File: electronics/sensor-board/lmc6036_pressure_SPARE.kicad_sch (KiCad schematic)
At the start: 17 parts, among them U15 LMC6036

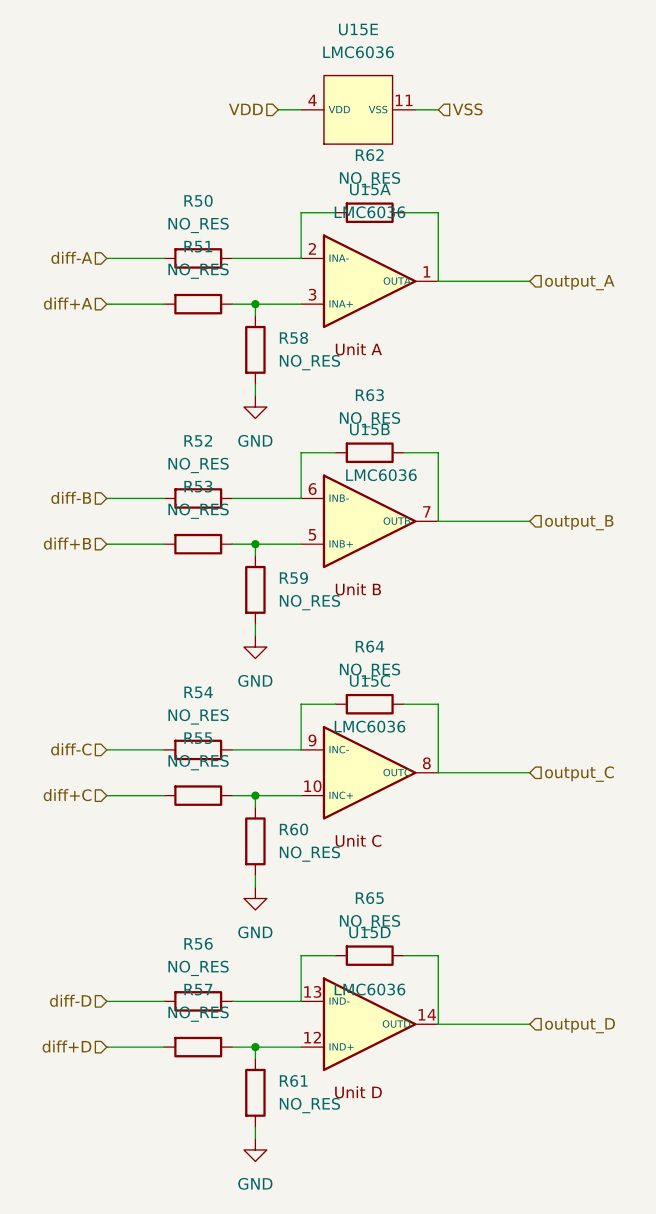
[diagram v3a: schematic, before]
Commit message: updated loadcell amplifier
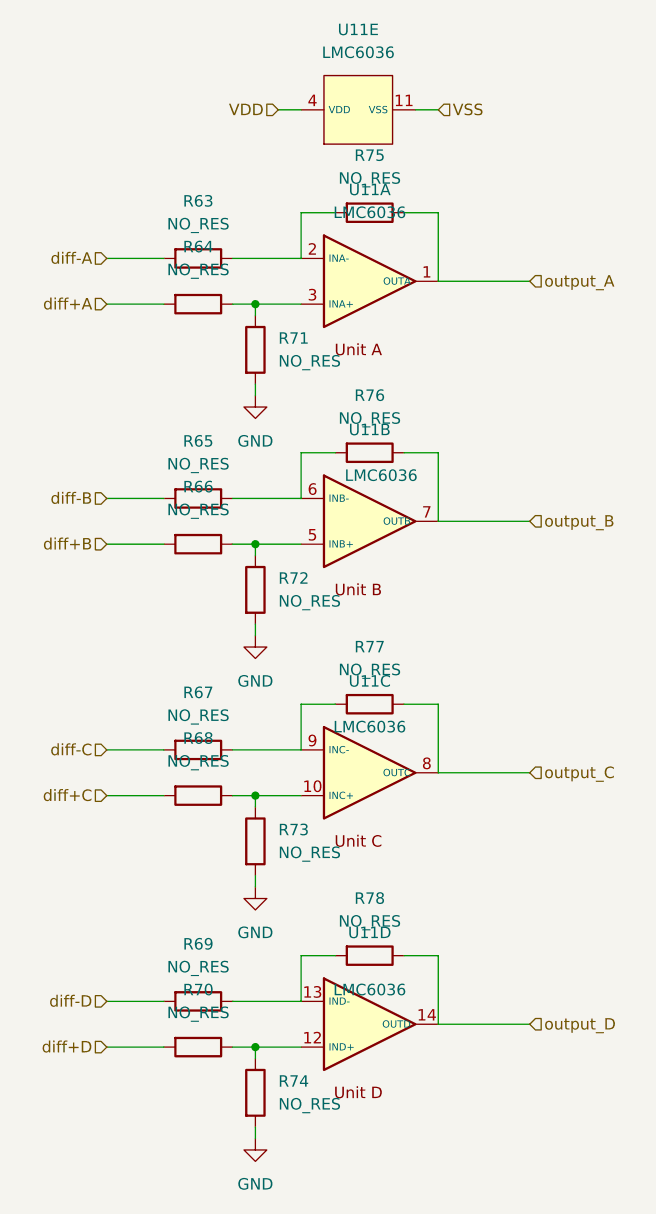
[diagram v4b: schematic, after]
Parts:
- renumbered R50 to R63, R51 to R64, R52 to R65, R53 to R66, R54 to R67, R55 to R68, R56 to R69, R57 to R70, R58 to R71, R59 to R72, R60 to R73, R61 to R74, R62 to R75, R63 to R76, R64 to R77, R65 to R78, U15 to U11
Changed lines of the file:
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@@
   (symbol (lib_id "LMC6036_custom:LMC6036") (at 153.67 63.5 0) (unit 1)
     (in_bom yes) (on_board yes) (fields_autoplaced)
-    (property "Reference" "U15" (id 0) (at 154.94 53.34 0))
+    (property "Reference" "U11" (id 0) (at 154.94 53.34 0))
     (property "Value" "LMC6036" (id 1) (at 154.94 55.88 0))
     (property "Footprint" "LMC6036:SOP65P640X120-14N" (id 2) (at 155.575 63.5 0)
@@
   (symbol (lib_id "Device:R") (at 154.94 55.88 270) (unit 1)
     (in_bom yes) (on_board yes) (fields_autoplaced)
-    (property "Reference" "R62" (id 0) (at 154.94 49.53 90))
+    (property "Reference" "R75" (id 0) (at 154.94 49.53 90))
     (property "Value" "NO_RES" (id 1) (at 154.94 52.07 90))
     (property "Footprint" "Resistor_SMD:R_0603_1608Metric" (id 2) (at 154.94 54.102 90)
@@
   (symbol (lib_id "Device:R") (at 135.89 87.63 270) (unit 1)
     (in_bom yes) (on_board yes) (fields_autoplaced)
-    (property "Reference" "R52" (id 0) (at 135.89 81.28 90))
+    (property "Reference" "R65" (id 0) (at 135.89 81.28 90))
     (property "Value" "NO_RES" (id 1) (at 135.89 83.82 90))
     (property "Footprint" "Resistor_SMD:R_0603_1608Metric" (id 2) (at 135.89 85.852 90)
@@
   (symbol (lib_id "LMC6036_custom:LMC6036") (at 153.67 146.05 0) (unit 4)
     (in_bom yes) (on_board yes)
-    (property "Reference" "U15" (id 0) (at 154.94 135.89 0))
+    (property "Reference" "U11" (id 0) (at 154.94 135.89 0))
     (property "Value" "LMC6036" (id 1) (at 154.94 142.24 0))
     (property "Footprint" "LMC6036:SOP65P640X120-14N" (id 2) (at 155.575 146.05 0)
@@
   (symbol (lib_id "power:GND") (at 142.24 76.2 0) (unit 1)
     (in_bom yes) (on_board yes) (fields_autoplaced)
-    (property "Reference" "#PWR0115" (id 0) (at 142.24 82.55 0)
+    (property "Reference" "#PWR0134" (id 0) (at 142.24 82.55 0)
       (effects (font (size 1.27 1.27)) hide)
     )
@@
   (symbol (lib_id "LMC6036_custom:LMC6036") (at 153.67 118.11 0) (unit 3)
     (in_bom yes) (on_board yes)
-    (property "Reference" "U15" (id 0) (at 154.94 107.95 0))
+    (property "Reference" "U11" (id 0) (at 154.94 107.95 0))
     (property "Value" "LMC6036" (id 1) (at 154.94 113.03 0))
     (property "Footprint" "LMC6036:SOP65P640X120-14N" (id 2) (at 155.575 118.11 0)
@@
   (symbol (lib_id "Device:R") (at 135.89 143.51 270) (unit 1)
     (in_bom yes) (on_board yes) (fields_autoplaced)
-    (property "Reference" "R56" (id 0) (at 135.89 137.16 90))
+    (property "Reference" "R69" (id 0) (at 135.89 137.16 90))
     (property "Value" "NO_RES" (id 1) (at 135.89 139.7 90))
     (property "Footprint" "Resistor_SMD:R_0603_1608Metric" (id 2) (at 135.89 141.732 90)
@@
   (symbol (lib_id "Device:R") (at 142.24 97.79 0) (unit 1)
     (in_bom yes) (on_board yes) (fields_autoplaced)
-    (property "Reference" "R59" (id 0) (at 144.78 96.5199 0)
+    (property "Reference" "R72" (id 0) (at 144.78 96.5199 0)
       (effects (font (size 1.27 1.27)) (justify left))
     )
@@
   (symbol (lib_id "power:GND") (at 142.24 102.87 0) (unit 1)
     (in_bom yes) (on_board yes) (fields_autoplaced)
-    (property "Reference" "#PWR0116" (id 0) (at 142.24 109.22 0)
+    (property "Reference" "#PWR0135" (id 0) (at 142.24 109.22 0)
       (effects (font (size 1.27 1.27)) hide)
     )
@@
   (symbol (lib_id "power:GND") (at 142.24 158.75 0) (unit 1)
     (in_bom yes) (on_board yes) (fields_autoplaced)
-    (property "Reference" "#PWR0118" (id 0) (at 142.24 165.1 0)
+    (property "Reference" "#PWR0137" (id 0) (at 142.24 165.1 0)
       (effects (font (size 1.27 1.27)) hide)
     )
@@
   (symbol (lib_id "Device:R") (at 142.24 71.12 0) (unit 1)
     (in_bom yes) (on_board yes) (fields_autoplaced)
-    (property "Reference" "R58" (id 0) (at 144.78 69.8499 0)
+    (property "Reference" "R71" (id 0) (at 144.78 69.8499 0)
       (effects (font (size 1.27 1.27)) (justify left))
     )
@@
   (symbol (lib_id "Device:R") (at 135.89 66.04 270) (unit 1)
     (in_bom yes) (on_board yes) (fields_autoplaced)
-    (property "Reference" "R51" (id 0) (at 135.89 59.69 90))
+    (property "Reference" "R64" (id 0) (at 135.89 59.69 90))
     (property "Value" "NO_RES" (id 1) (at 135.89 62.23 90))
     (property "Footprint" "Resistor_SMD:R_0603_1608Metric" (id 2) (at 135.89 64.262 90)
@@
   (symbol (lib_id "LMC6036_custom:LMC6036") (at 153.67 90.17 0) (unit 2)
     (in_bom yes) (on_board yes)
-    (property "Reference" "U15" (id 0) (at 154.94 80.01 0))
+    (property "Reference" "U11" (id 0) (at 154.94 80.01 0))
     (property "Value" "LMC6036" (id 1) (at 156.21 85.09 0))
     (property "Footprint" "LMC6036:SOP65P640X120-14N" (id 2) (at 155.575 90.17 0)
@@
   (symbol (lib_id "Device:R") (at 154.94 110.49 270) (unit 1)
     (in_bom yes) (on_board yes) (fields_autoplaced)
-    (property "Reference" "R64" (id 0) (at 154.94 104.14 90))
+    (property "Reference" "R77" (id 0) (at 154.94 104.14 90))
     (property "Value" "NO_RES" (id 1) (at 154.94 106.68 90))
     (property "Footprint" "Resistor_SMD:R_0603_1608Metric" (id 2) (at 154.94 108.712 90)
@@
   (symbol (lib_id "Device:R") (at 142.24 125.73 0) (unit 1)
     (in_bom yes) (on_board yes) (fields_autoplaced)
-    (property "Reference" "R60" (id 0) (at 144.78 124.4599 0)
+    (property "Reference" "R73" (id 0) (at 144.78 124.4599 0)
       (effects (font (size 1.27 1.27)) (justify left))
     )
@@
   (symbol (lib_id "Device:R") (at 135.89 92.71 270) (unit 1)
     (in_bom yes) (on_board yes) (fields_autoplaced)
-    (property "Reference" "R53" (id 0) (at 135.89 86.36 90))
+    (property "Reference" "R66" (id 0) (at 135.89 86.36 90))
     (property "Value" "NO_RES" (id 1) (at 135.89 88.9 90))
     (property "Footprint" "Resistor_SMD:R_0603_1608Metric" (id 2) (at 135.89 90.932 90)
@@
   (symbol (lib_id "LMC6036_custom:LMC6036") (at 153.67 44.45 90) (unit 5)
     (in_bom yes) (on_board yes) (fields_autoplaced)
-    (property "Reference" "U15" (id 0) (at 153.67 35.56 90))
+    (property "Reference" "U11" (id 0) (at 153.67 35.56 90))
     (property "Value" "LMC6036" (id 1) (at 153.67 38.1 90))
     (property "Footprint" "LMC6036:SOP65P640X120-14N" (id 2) (at 153.67 42.545 0)
@@
   (symbol (lib_id "Device:R") (at 135.89 115.57 270) (unit 1)
     (in_bom yes) (on_board yes) (fields_autoplaced)
-    (property "Reference" "R54" (id 0) (at 135.89 109.22 90))
+    (property "Reference" "R67" (id 0) (at 135.89 109.22 90))
     (property "Value" "NO_RES" (id 1) (at 135.89 111.76 90))
     (property "Footprint" "Resistor_SMD:R_0603_1608Metric" (id 2) (at 135.89 113.792 90)
@@
   (symbol (lib_id "power:GND") (at 142.24 130.81 0) (unit 1)
     (in_bom yes) (on_board yes) (fields_autoplaced)
-    (property "Reference" "#PWR0117" (id 0) (at 142.24 137.16 0)
+    (property "Reference" "#PWR0136" (id 0) (at 142.24 137.16 0)
       (effects (font (size 1.27 1.27)) hide)
     )
@@
   (symbol (lib_id "Device:R") (at 142.24 153.67 0) (unit 1)
     (in_bom yes) (on_board yes) (fields_autoplaced)
-    (property "Reference" "R61" (id 0) (at 144.78 152.3999 0)
+    (property "Reference" "R74" (id 0) (at 144.78 152.3999 0)
       (effects (font (size 1.27 1.27)) (justify left))
     )
@@
   (symbol (lib_id "Device:R") (at 154.94 82.55 270) (unit 1)
     (in_bom yes) (on_board yes) (fields_autoplaced)
-    (property "Reference" "R63" (id 0) (at 154.94 76.2 90))
+    (property "Reference" "R76" (id 0) (at 154.94 76.2 90))
     (property "Value" "NO_RES" (id 1) (at 154.94 78.74 90))
     (property "Footprint" "Resistor_SMD:R_0603_1608Metric" (id 2) (at 154.94 80.772 90)
@@
   (symbol (lib_id "Device:R") (at 154.94 138.43 270) (unit 1)
     (in_bom yes) (on_board yes) (fields_autoplaced)
-    (property "Reference" "R65" (id 0) (at 154.94 132.08 90))
+    (property "Reference" "R78" (id 0) (at 154.94 132.08 90))
     (property "Value" "NO_RES" (id 1) (at 154.94 134.62 90))
     (property "Footprint" "Resistor_SMD:R_0603_1608Metric" (id 2) (at 154.94 136.652 90)
@@
   (symbol (lib_id "Device:R") (at 135.89 60.96 270) (unit 1)
     (in_bom yes) (on_board yes) (fields_autoplaced)
-    (property "Reference" "R50" (id 0) (at 135.89 54.61 90))
+    (property "Reference" "R63" (id 0) (at 135.89 54.61 90))
     (property "Value" "NO_RES" (id 1) (at 135.89 57.15 90))
     (property "Footprint" "Resistor_SMD:R_0603_1608Metric" (id 2) (at 135.89 59.182 90)
@@
   (symbol (lib_id "Device:R") (at 135.89 148.59 270) (unit 1)
     (in_bom yes) (on_board yes) (fields_autoplaced)
-    (property "Reference" "R57" (id 0) (at 135.89 142.24 90))
+    (property "Reference" "R70" (id 0) (at 135.89 142.24 90))
     (property "Value" "NO_RES" (id 1) (at 135.89 144.78 90))
     (property "Footprint" "Resistor_SMD:R_0603_1608Metric" (id 2) (at 135.89 146.812 90)
@@
   (symbol (lib_id "Device:R") (at 135.89 120.65 270) (unit 1)
     (in_bom yes) (on_board yes) (fields_autoplaced)
-    (property "Reference" "R55" (id 0) (at 135.89 114.3 90))
+    (property "Reference" "R68" (id 0) (at 135.89 114.3 90))
     (property "Value" "NO_RES" (id 1) (at 135.89 116.84 90))
     (property "Footprint" "Resistor_SMD:R_0603_1608Metric" (id 2) (at 135.89 118.872 90)

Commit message: Work on sensor-board pcb
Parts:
- added J?: Spare_4, Custom_Molex_SL_2.54:SL_2.54_H_2pin, symbol Connector_Generic:Conn_01x02
- added J?: Spare_1, Custom_Molex_SL_2.54:SL_2.54_H_2pin, symbol Connector_Generic:Conn_01x02
- added J?: Spare_2, Custom_Molex_SL_2.54:SL_2.54_H_2pin, symbol Connector_Generic:Conn_01x02
- added J?: Spare_HR_2, Custom_Molex_SL_2.54:SL_2.54_H_4pin, symbol Connector_Generic:Conn_01x04
- added J?: Spare_3, Custom_Molex_SL_2.54:SL_2.54_H_2pin, symbol Connector_Generic:Conn_01x02
- added J?: Spare_HR_1, Custom_Molex_SL_2.54:SL_2.54_H_4pin, symbol Connector_Generic:Conn_01x04
- added TP? (x4): TestPoint, TestPoint:TestPoint_Pad_D2.0mm, symbol Connector:TestPoint
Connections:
- net GND: now also J?.1 (Pin_1), J?.1 (Pin_1)
- new net +12V: J?.4 (Pin_4), J?.4 (Pin_4)
